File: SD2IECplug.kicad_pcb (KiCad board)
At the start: 2 copper layers, 50 x 49.4 mm, 49 parts, among them J1 ISP, J2 X6, J3 Aux, J4 IEC, J5 C64-CassettePort, J6 C64-CassettePort, J7 Power, J8 X3, Q1 IRLML2803, Q2 IRLML2803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

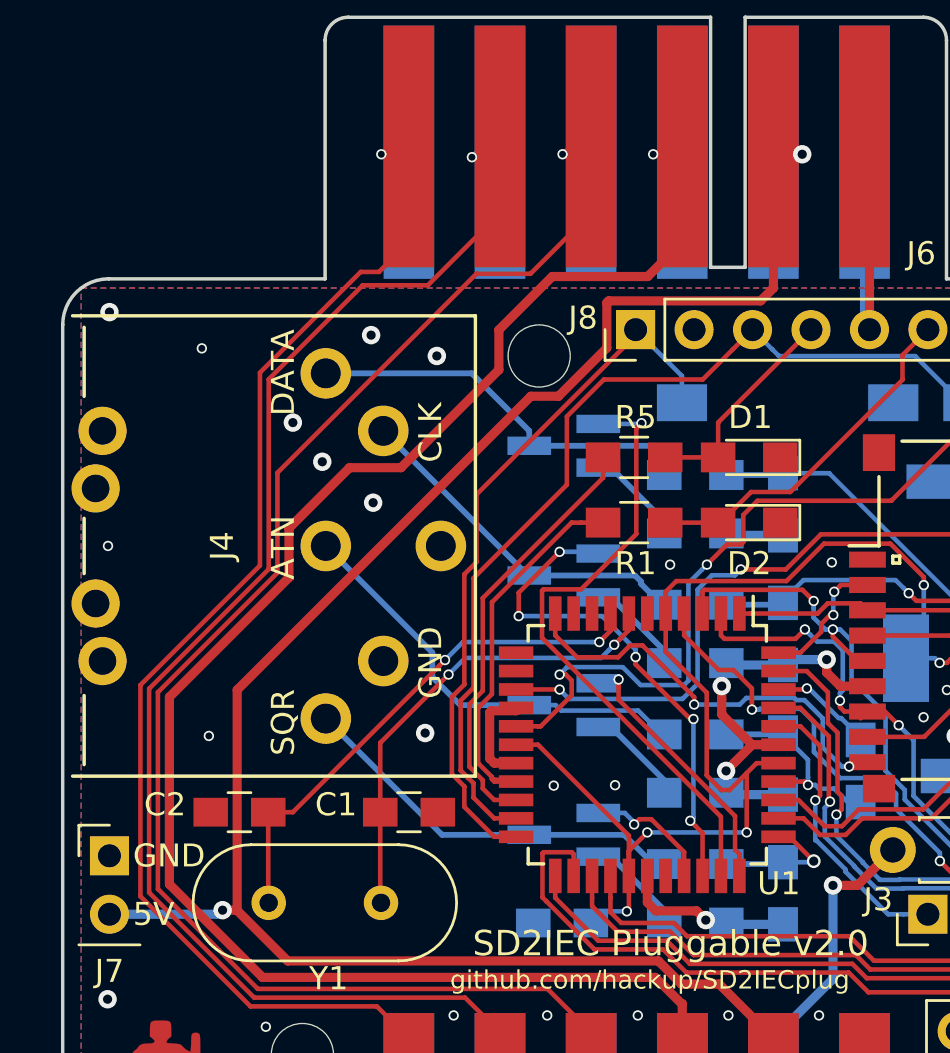
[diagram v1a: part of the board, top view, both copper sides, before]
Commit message: Moved data lines further away from drill holes.
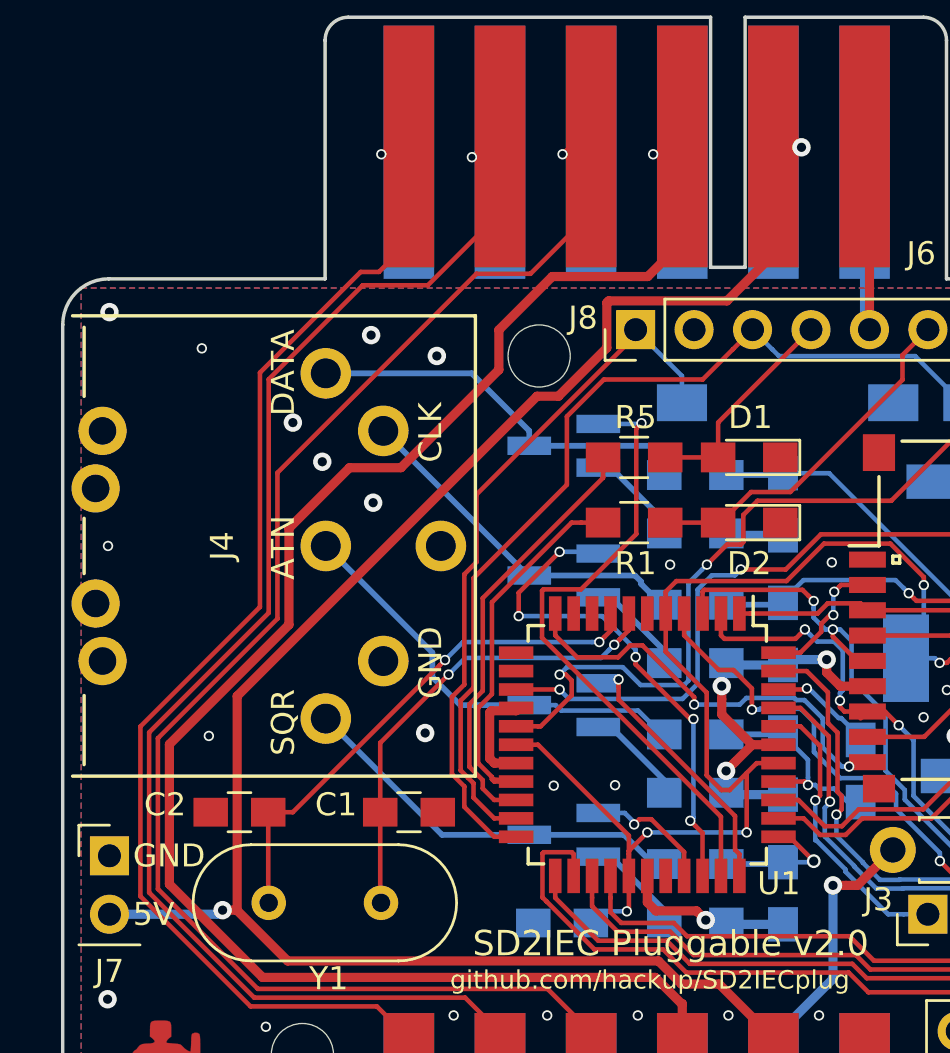
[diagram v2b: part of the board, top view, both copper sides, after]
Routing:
- net Cas-5V: track 94.7 -> 93.9 mm
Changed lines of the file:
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@@
     (36 B.SilkS user)
     (37 F.SilkS user)
-    (38 B.Mask user)
-    (39 F.Mask user)
+    (38 B.Mask user hide)
+    (39 F.Mask user hide)
     (40 Dwgs.User user)
     (41 Cmts.User user)
@@
   (segment (start 126.84 55.35) (end 127.052 55.562) (width 0.4) (layer B.Cu) (net 25))
   (segment (start 126.84 47.854) (end 126.84 55.35) (width 0.4) (layer B.Cu) (net 25))
-  (via (at 124.131 47.942) (size 0.8) (drill 0.4) (layers F.Cu B.Cu) (net 26))
-  (segment (start 122.88 47.854) (end 124.043 47.854) (width 0.4) (layer B.Cu) (net 26))
-  (segment (start 124.043 47.854) (end 124.131 47.942) (width 0.4) (layer B.Cu) (net 26))
-  (segment (start 122.968 47.942) (end 122.88 47.854) (width 0.4) (layer F.Cu) (net 26))
-  (segment (start 124.131 47.942) (end 122.968 47.942) (width 0.4) (layer F.Cu) (net 26))
-  (segment (start 99.580001 80.797003) (end 99.580001 71.215997) (width 0.4) (layer F.Cu) (net 26))
   (segment (start 126.033426 79.707332) (end 125.467741 79.707332) (width 0.4) (layer F.Cu) (net 26))
   (segment (start 126.528668 79.707332) (end 126.033426 79.707332) (width 0.4) (layer F.Cu) (net 26))
   (segment (start 128.068 78.168) (end 126.528668 79.707332) (width 0.4) (layer F.Cu) (net 26))
   (via (at 125.467741 79.707332) (size 0.8) (drill 0.4) (layers F.Cu B.Cu) (net 26))
-  (segment (start 122.322001 54.311999) (end 122.88 53.754) (width 0.4) (layer F.Cu) (net 26))
-  (segment (start 115.721999 54.311999) (end 122.322001 54.311999) (width 0.4) (layer F.Cu) (net 26))
-  (segment (start 122.88 53.754) (end 122.88 47.854) (width 0.4) (layer F.Cu) (net 26))
-  (segment (start 115.641999 54.391999) (end 115.721999 54.311999) (width 0.4) (layer F.Cu) (net 26))
-  (segment (start 115.641999 56.354003) (end 115.641999 54.391999) (width 0.4) (layer F.Cu) (net 26))
-  (segment (start 112.340997 58.455001) (end 113.541001 58.455001) (width 0.4) (layer F.Cu) (net 26))
-  (segment (start 99.580001 71.215997) (end 112.340997 58.455001) (width 0.4) (layer F.Cu) (net 26))
-  (segment (start 113.541001 58.455001) (end 115.641999 56.354003) (width 0.4) (layer F.Cu) (net 26))
   (via (at 98.9469 80.7842) (size 0.8) (drill 0.4) (layers F.Cu B.Cu) (net 26))
   (segment (start 99.567198 80.7842) (end 99.580001 80.797003) (width 0.4) (layer F.Cu) (net 26))
@@
   (segment (start 120.521989 83.995989) (end 118.886531 83.995989) (width 0.4) (layer F.Cu) (net 26))
   (segment (start 122.88 87.754) (end 122.88 86.354) (width 0.4) (layer F.Cu) (net 26))
+  (segment (start 99.580001 71.482541) (end 112.607541 58.455001) (width 0.4) (layer F.Cu) (net 26))
+  (segment (start 99.580001 80.797003) (end 99.580001 71.482541) (width 0.4) (layer F.Cu) (net 26))
+  (segment (start 112.607541 58.455001) (end 113.541001 58.455001) (width 0.4) (layer F.Cu) (net 26))
+  (segment (start 113.541001 58.455001) (end 115.641999 56.354003) (width 0.4) (layer F.Cu) (net 26))
+  (via (at 124.099 47.639) (size 0.8) (drill 0.4) (layers F.Cu B.Cu) (net 26))
+  (segment (start 122.88 47.604) (end 124.064 47.604) (width 0.4) (layer F.Cu) (net 26))
+  (segment (start 124.064 47.604) (end 124.099 47.639) (width 0.4) (layer F.Cu) (net 26))
+  (segment (start 123.095 47.639) (end 122.88 47.854) (width 0.4) (layer B.Cu) (net 26))
+  (segment (start 124.099 47.639) (end 123.095 47.639) (width 0.4) (layer B.Cu) (net 26))
+  (segment (start 115.641999 54.391999) (end 115.641999 56.354003) (width 0.4) (layer F.Cu) (net 26))
+  (segment (start 115.721999 54.311999) (end 115.641999 54.391999) (width 0.4) (layer F.Cu) (net 26))
+  (segment (start 120.863766 54.311999) (end 115.721999 54.311999) (width 0.4) (layer F.Cu) (net 26))
+  (segment (start 122.88 52.295765) (end 120.863766 54.311999) (width 0.4) (layer F.Cu) (net 26))
+  (segment (start 122.88 47.604) (end 122.88 52.295765) (width 0.4) (layer F.Cu) (net 26))
   (via (at 117.654 47.942) (size 0.45) (drill 0.3) (layers F.Cu B.Cu) (net 27))
   (segment (start 118.92 47.854) (end 117.742 47.854) (width 0.2) (layer F.Cu) (net 27))
@@
   (segment (start 106.698001 61.560001) (end 104.461997 61.560001) (width 0.4) (layer F.Cu) (net 27))
   (segment (start 104.461997 61.560001) (end 101.829999 64.191999) (width 0.4) (layer F.Cu) (net 27))
-  (segment (start 101.829999 64.191999) (end 101.829999 66.331399) (width 0.4) (layer F.Cu) (net 27))
-  (segment (start 101.829999 66.331399) (end 96.6355 71.525898) (width 0.4) (layer F.Cu) (net 27))
   (segment (start 96.6355 79.656802) (end 100.683898 83.7052) (width 0.4) (layer F.Cu) (net 27))
-  (segment (start 96.6355 71.525898) (end 96.6355 79.656802) (width 0.4) (layer F.Cu) (net 27))
   (segment (start 117.7472 83.7052) (end 118.892 84.85) (width 0.4) (layer F.Cu) (net 27))
   (segment (start 118.916 84.85) (end 118.92 84.854) (width 0.4) (layer F.Cu) (net 27))
   (segment (start 100.683898 83.7052) (end 117.7472 83.7052) (width 0.4) (layer F.Cu) (net 27))
   (via (at 118.92 87.754) (size 0.8) (drill 0.4) (layers F.Cu B.Cu) (net 27))
+  (segment (start 101.829999 64.191999) (end 101.829999 68.384001) (width 0.4) (layer F.Cu) (net 27))
+  (segment (start 96.6355 73.5785) (end 96.6355 79.656802) (width 0.4) (layer F.Cu) (net 27))
+  (segment (start 101.829999 68.384001) (end 96.6355 73.5785) (width 0.4) (layer F.Cu) (net 27))
   (via (at 113.717 47.942) (size 0.45) (drill 0.3) (layers F.Cu B.Cu) (net 28))
   (segment (start 114.055 47.604) (end 113.717 47.942) (width 0.2) (layer F.Cu) (net 28))
@@
   (segment (start 113.717 47.942) (end 114.872 47.942) (width 0.2) (layer B.Cu) (net 28))
   (segment (start 100.476787 84.205211) (end 96.13549 79.863914) (width 0.2) (layer F.Cu) (net 28))
-  (segment (start 96.13549 71.318786) (end 101.329988 66.124288) (width 0.2) (layer F.Cu) (net 28))
   (segment (start 112.324001 53.134001) (end 114.96 50.498002) (width 0.2) (layer F.Cu) (net 28))
   (segment (start 101.329988 61.780014) (end 109.976001 53.134001) (width 0.2) (layer F.Cu) (net 28))
   (segment (start 109.976001 53.134001) (end 112.324001 53.134001) (width 0.2) (layer F.Cu) (net 28))
-  (segment (start 101.329988 66.124288) (end 101.329988 61.780014) (width 0.2) (layer F.Cu) (net 28))
-  (segment (start 96.13549 79.863914) (end 96.13549 71.318786) (width 0.2) (layer F.Cu) (net 28))
   (segment (start 113.065211 84.205211) (end 100.476787 84.205211) (width 0.2) (layer F.Cu) (net 28))
   (segment (start 114.96 86.1) (end 113.065211 84.205211) (width 0.2) (layer F.Cu) (net 28))
   (via (at 114.96 87.754) (size 0.45) (drill 0.3) (layers F.Cu B.Cu) (net 28))
+  (segment (start 101.329988 61.780014) (end 101.329988 68.122012) (width 0.2) (layer F.Cu) (net 28))
+  (segment (start 96.13549 73.31651) (end 96.13549 79.863914) (width 0.2) (layer F.Cu) (net 28))
+  (segment (start 101.329988 68.122012) (end 96.13549 73.31651) (width 0.2) (layer F.Cu) (net 28))
   (via (at 109.78 48.069) (size 0.45) (drill 0.3) (layers F.Cu B.Cu) (net 29))
   (segment (start 109.995 47.854) (end 109.78 48.069) (width 0.2) (layer B.Cu) (net 29))
@@
   (segment (start 109.78 48.069) (end 110.535 48.069) (width 0.2) (layer F.Cu) (net 29))
   (segment (start 111 87.5) (end 111 86.1) (width 0.2) (layer F.Cu) (net 29))
-  (segment (start 95.75548 80.02132) (end 95.75548 71.16138) (width 0.2) (layer F.Cu) (net 29))
-  (segment (start 95.75548 71.16138) (end 100.949977 65.966883) (width 0.2) (layer F.Cu) (net 29))
   (segment (start 100.949978 57.72002) (end 105.035997 53.634001) (width 0.2) (layer F.Cu) (net 29))
   (segment (start 111 86.1) (end 109.485222 84.585222) (width 0.2) (layer F.Cu) (net 29))
@@
   (segment (start 109.485222 84.585222) (end 100.319382 84.585222) (width 0.2) (layer F.Cu) (net 29))
   (segment (start 111 50.498002) (end 111 47.604) (width 0.2) (layer F.Cu) (net 29))
-  (segment (start 100.949977 65.966883) (end 100.949978 57.72002) (width 0.2) (layer F.Cu) (net 29))
   (segment (start 100.319382 84.585222) (end 95.75548 80.02132) (width 0.2) (layer F.Cu) (net 29))
   (via (at 111 87.754) (size 0.45) (drill 0.3) (layers F.Cu B.Cu) (net 29))
+  (segment (start 100.949978 57.72002) (end 100.949978 67.867022) (width 0.2) (layer F.Cu) (net 29))
+  (segment (start 95.75548 73.06152) (end 95.75548 80.02132) (width 0.2) (layer F.Cu) (net 29))
+  (segment (start 100.949978 67.867022) (end 95.75548 73.06152) (width 0.2) (layer F.Cu) (net 29))
   (via (at 105.843 47.942) (size 0.45) (drill 0.3) (layers F.Cu B.Cu) (net 30))
   (segment (start 106.181 47.604) (end 105.843 47.942) (width 0.2) (layer F.Cu) (net 30))
@@
   (segment (start 100.161977 84.965233) (end 105.651233 84.965233) (width 0.2) (layer F.Cu) (net 30))
   (segment (start 95.37547 80.178726) (end 100.161977 84.965233) (width 0.2) (layer F.Cu) (net 30))
-  (segment (start 95.37547 71.003974) (end 95.37547 80.178726) (width 0.2) (layer F.Cu) (net 30))
   (segment (start 107.04 47.604) (end 107.04 51.754) (width 0.2) (layer F.Cu) (net 30))
   (segment (start 107.04 51.754) (end 105.74 53.054) (width 0.2) (layer F.Cu) (net 30))
   (segment (start 105.74 53.054) (end 104.946 53.054) (width 0.2) (layer F.Cu) (net 30))
   (segment (start 104.946 53.054) (end 100.569968 57.430032) (width 0.2) (layer F.Cu) (net 30))
-  (segment (start 100.569968 57.430032) (end 100.569967 65.809477) (width 0.2) (layer F.Cu) (net 30))
-  (segment (start 100.569967 65.809477) (end 95.37547 71.003974) (width 0.2) (layer F.Cu) (net 30))
+  (segment (start 100.569968 57.430032) (end 100.569968 67.612032) (width 0.2) (layer F.Cu) (net 30))
+  (segment (start 95.37547 72.80653) (end 95.37547 80.178726) (width 0.2) (layer F.Cu) (net 30))
+  (segment (start 100.569968 67.612032) (end 95.37547 72.80653) (width 0.2) (layer F.Cu) (net 30))
   (segment (start 120.478 63.946) (end 118.178 63.946) (width 0.2) (layer F.Cu) (net 31))
   (segment (start 121.908012 62.615988) (end 120.578 63.946) (width 0.2) (layer F.Cu) (net 31))

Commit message: Revision increment.
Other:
- board text added: "SD2IEC Pluggable v2.1"
- board text removed: "SD2IEC Pluggable v2.0"
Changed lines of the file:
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@@
   (title_block
     (title "SD2IEC Pluggable")
-    (date 2018-09-12)
-    (rev 2.0)
+    (date 2018-10-08)
+    (rev 2.1)
     (company www.hackup.net)
   )
@@
   (gr_line (start 130.4 53.354) (end 130.4 42.989) (angle 90) (layer Edge.Cuts) (width 0.15))
   (gr_arc (start 94 55.354) (end 92 55.354) (angle 90) (layer Edge.Cuts) (width 0.15))
-  (gr_text "SD2IEC Pluggable v2.0" (at 118.416 82.232) (layer F.SilkS)
+  (gr_text "SD2IEC Pluggable v2.1" (at 118.416 82.232) (layer F.SilkS)
     (effects (font (size 1.1 1.1) (thickness 0.22)))
   )

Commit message: Improved ziptie holes.
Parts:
- MH1, MH2: footprint DIN-Connectors:ZipTie_2.7mm -> DIN-Connectors:ZipTie_3.0mm
- moved MH1 0.50 mm to (97.0, 62.1)
- moved MH2 0.50 mm to (97.0, 67.9)
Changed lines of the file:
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@@
     (pad "" thru_hole circle (at -2.5 -10 90) (size 2.1 2.1) (drill 1.2) (layers *.Cu *.Mask))
-  )
-  (module DIN-Connectors:ZipTie_2.7mm (layer F.Cu)
-    (at 97 62.6)
-    (descr "Mounting Hole 2.7mm, no annular")
-    (tags "mounting hole 2.7mm no annular")
-    (attr virtual)
-    (fp_text reference MH1 (at 0 -1.778) (layer F.SilkS) hide
-      (effects (font (size 1 1) (thickness 0.15)))
-    )
-    (fp_text value ZipTie (at 0 1.905) (layer F.Fab) hide
-      (effects (font (size 1 1) (thickness 0.15)))
-    )
-    (fp_arc (start -1.143 0) (end -1.143 -1.016) (angle -180) (layer F.CrtYd) (width 0.07))
-    (fp_arc (start 1.143 0) (end 1.143 1.016) (angle -180) (layer F.CrtYd) (width 0.07))
-    (fp_line (start -1.143 1.016) (end 1.143 1.016) (layer F.CrtYd) (width 0.07))
-    (fp_line (start -1.143 -1.016) (end 1.143 -1.016) (layer F.CrtYd) (width 0.07))
-    (fp_arc (start -0.889 0) (end -0.889 -0.762) (angle -180) (layer Cmts.User) (width 0.15))
-    (fp_arc (start 0.889 0) (end 0.889 0.762) (angle -180) (layer Cmts.User) (width 0.15))
-    (fp_line (start -0.889 0.762) (end 0.889 0.762) (layer Cmts.User) (width 0.15))
-    (fp_line (start -0.889 -0.762) (end 0.889 -0.762) (layer Cmts.User) (width 0.15))
-    (fp_text user %R (at 0.3 0) (layer F.Fab)
-      (effects (font (size 1 1) (thickness 0.15)))
-    )
-    (pad "" np_thru_hole oval (at 0 0) (size 2.7 1.1) (drill oval 2.7 1.1) (layers *.Cu *.Mask))
-  )
-  (module DIN-Connectors:ZipTie_2.7mm (layer F.Cu)
-    (at 97 67.4)
-    (descr "Mounting Hole 2.7mm, no annular")
-    (tags "mounting hole 2.7mm no annular")
-    (attr virtual)
-    (fp_text reference MH2 (at 0 -1.778) (layer F.SilkS) hide
-      (effects (font (size 1 1) (thickness 0.15)))
-    )
-    (fp_text value ZipTie (at 0 1.905) (layer F.Fab) hide
-      (effects (font (size 1 1) (thickness 0.15)))
-    )
-    (fp_text user %R (at 0.3 0) (layer F.Fab)
-      (effects (font (size 1 1) (thickness 0.15)))
-    )
-    (fp_line (start -0.889 -0.762) (end 0.889 -0.762) (layer Cmts.User) (width 0.15))
-    (fp_line (start -0.889 0.762) (end 0.889 0.762) (layer Cmts.User) (width 0.15))
-    (fp_arc (start 0.889 0) (end 0.889 0.762) (angle -180) (layer Cmts.User) (width 0.15))
-    (fp_arc (start -0.889 0) (end -0.889 -0.762) (angle -180) (layer Cmts.User) (width 0.15))
-    (fp_line (start -1.143 -1.016) (end 1.143 -1.016) (layer F.CrtYd) (width 0.07))
-    (fp_line (start -1.143 1.016) (end 1.143 1.016) (layer F.CrtYd) (width 0.07))
-    (fp_arc (start 1.143 0) (end 1.143 1.016) (angle -180) (layer F.CrtYd) (width 0.07))
-    (fp_arc (start -1.143 0) (end -1.143 -1.016) (angle -180) (layer F.CrtYd) (width 0.07))
-    (pad "" np_thru_hole oval (at 0 0) (size 2.7 1.1) (drill oval 2.7 1.1) (layers *.Cu *.Mask))
   )
   (module Pin_Headers:Pin_Header_Straight_1x03_Pitch2.54mm (layer F.Cu)
@@
     )
   )
+  (module DIN-Connectors:ZipTie_3.0mm (layer F.Cu)
+    (at 97 62.1)
+    (descr "Mounting Hole 2.7mm, no annular")
+    (tags "mounting hole 2.7mm no annular")
+    (attr virtual)
+    (fp_text reference MH1 (at 0 -1.778) (layer F.SilkS) hide
+      (effects (font (size 1 1) (thickness 0.15)))
+    )
+    (fp_text value ZipTie (at 0 1.905) (layer F.Fab)
+      (effects (font (size 1 1) (thickness 0.15)))
+    )
+    (fp_arc (start -1.143 0) (end -1.143 -1.016) (angle -180) (layer F.CrtYd) (width 0.07))
+    (fp_arc (start 1.143 0) (end 1.143 1.016) (angle -180) (layer F.CrtYd) (width 0.07))
+    (fp_line (start -1.143 1.016) (end 1.143 1.016) (layer F.CrtYd) (width 0.07))
+    (fp_line (start -1.143 -1.016) (end 1.143 -1.016) (layer F.CrtYd) (width 0.07))
+    (fp_arc (start -0.889 0) (end -0.889 -0.762) (angle -180) (layer Cmts.User) (width 0.15))
+    (fp_arc (start 0.889 0) (end 0.889 0.762) (angle -180) (layer Cmts.User) (width 0.15))
+    (fp_line (start -0.889 0.762) (end 0.889 0.762) (layer Cmts.User) (width 0.15))
+    (fp_line (start -0.889 -0.762) (end 0.889 -0.762) (layer Cmts.User) (width 0.15))
+    (fp_text user %R (at 0.3 0) (layer F.Fab)
+      (effects (font (size 1 1) (thickness 0.15)))
+    )
+    (pad "" np_thru_hole oval (at 0 0) (size 3.2 1.5) (drill oval 2.7 1.1) (layers *.Cu *.Mask))
+  )
+  (module DIN-Connectors:ZipTie_3.0mm (layer F.Cu)
+    (at 97 67.9)
+    (descr "Mounting Hole 2.7mm, no annular")
+    (tags "mounting hole 2.7mm no annular")
+    (attr virtual)
+    (fp_text reference MH2 (at 0 -1.778) (layer F.SilkS) hide
+      (effects (font (size 1 1) (thickness 0.15)))
+    )
+    (fp_text value ZipTie (at 0 1.905) (layer F.Fab)
+      (effects (font (size 1 1) (thickness 0.15)))
+    )
+    (fp_text user %R (at 0.3 0) (layer F.Fab)
+      (effects (font (size 1 1) (thickness 0.15)))
+    )
+    (fp_line (start -0.889 -0.762) (end 0.889 -0.762) (layer Cmts.User) (width 0.15))
+    (fp_line (start -0.889 0.762) (end 0.889 0.762) (layer Cmts.User) (width 0.15))
+    (fp_arc (start 0.889 0) (end 0.889 0.762) (angle -180) (layer Cmts.User) (width 0.15))
+    (fp_arc (start -0.889 0) (end -0.889 -0.762) (angle -180) (layer Cmts.User) (width 0.15))
+    (fp_line (start -1.143 -1.016) (end 1.143 -1.016) (layer F.CrtYd) (width 0.07))
+    (fp_line (start -1.143 1.016) (end 1.143 1.016) (layer F.CrtYd) (width 0.07))
+    (fp_arc (start 1.143 0) (end 1.143 1.016) (angle -180) (layer F.CrtYd) (width 0.07))
+    (fp_arc (start -1.143 0) (end -1.143 -1.016) (angle -180) (layer F.CrtYd) (width 0.07))
+    (pad "" np_thru_hole oval (at 0 0) (size 3.2 1.5) (drill oval 2.7 1.1) (layers *.Cu *.Mask))
+  )
   (gr_arc (start 142 73.604) (end 141.25 73.604) (angle -90) (layer Edge.Cuts) (width 0.15))

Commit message: IRLML2803 -> BSS138
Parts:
- Q1, Q2, Q3, Q4: value IRLML2803 -> BSS138
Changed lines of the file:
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@@
   )
   (layers
-    (0 F.Cu signal)
+    (0 F.Cu signal hide)
     (31 B.Cu signal)
     (32 B.Adhes user)
@@
       (effects (font (size 1 1) (thickness 0.15)) (justify mirror))
     )
-    (fp_text value IRLML2803 (at 0 -2.5 180) (layer B.Fab)
+    (fp_text value BSS138 (at 0 -2.5 180) (layer B.Fab)
       (effects (font (size 1 1) (thickness 0.15)) (justify mirror))
     )
@@
       (effects (font (size 1 1) (thickness 0.15)) (justify mirror))
     )
-    (fp_text value IRLML2803 (at 0 -2.5 180) (layer B.Fab)
+    (fp_text value BSS138 (at 0 -2.5 180) (layer B.Fab)
       (effects (font (size 1 1) (thickness 0.15)) (justify mirror))
     )
@@
       (effects (font (size 1 1) (thickness 0.15)) (justify mirror))
     )
-    (fp_text value IRLML2803 (at 0 -2.5 180) (layer B.Fab)
+    (fp_text value BSS138 (at 0 -2.5 180) (layer B.Fab)
       (effects (font (size 1 1) (thickness 0.15)) (justify mirror))
     )
@@
       (effects (font (size 1 1) (thickness 0.15)) (justify mirror))
     )
-    (fp_text value IRLML2803 (at 0 -2.5 180) (layer B.Fab)
-      (effects (font (size 1 1) (thickness 0.15)) (justify mirror))
-    )
+    (fp_text value BSS138 (at 0 -2.5 180) (layer B.Fab)
+      (effects (font (size 1 1) (thickness 0.15)) (justify mirror))
+    )
